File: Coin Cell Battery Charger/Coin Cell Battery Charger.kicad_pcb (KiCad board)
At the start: 4 copper layers, 120.2 x 120.2 mm, 40 parts, among them J1 0473461001, Q2 Q_PMOS_GSD, SW1 5176TRp, U1 BQ21040DBVR, U2 TLV74010PDBVR, U3 LTC6992CS6-3#TRMPBF, U4 AP2502KTR-G1, U5 AP2502KTR-G1, U6 LTC2954CTS8-1#TRMPBF

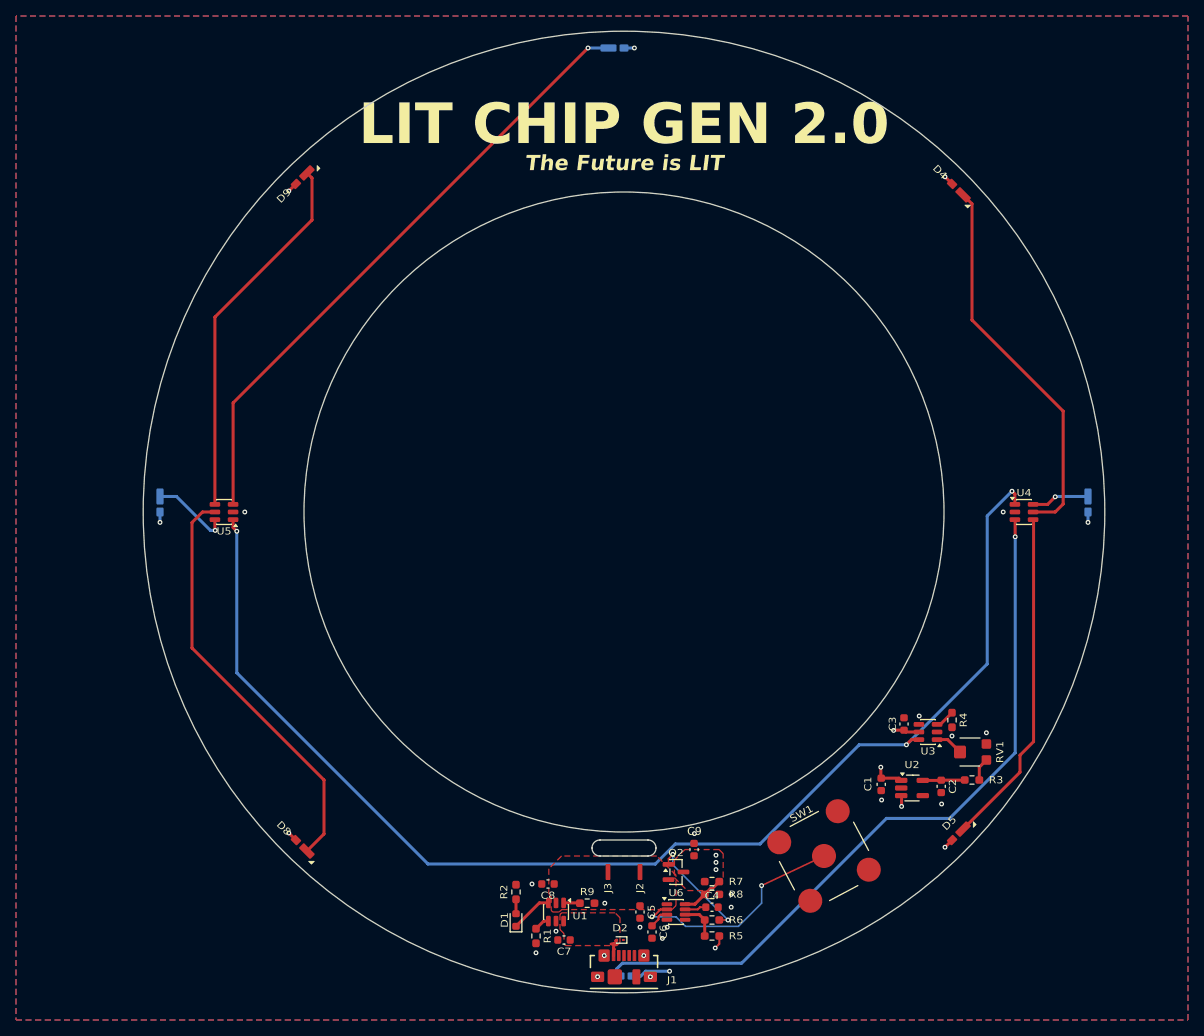
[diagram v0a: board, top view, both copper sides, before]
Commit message: Resized PCB to be 30mm OD, added vertical connector option, Electrical layout incomplete
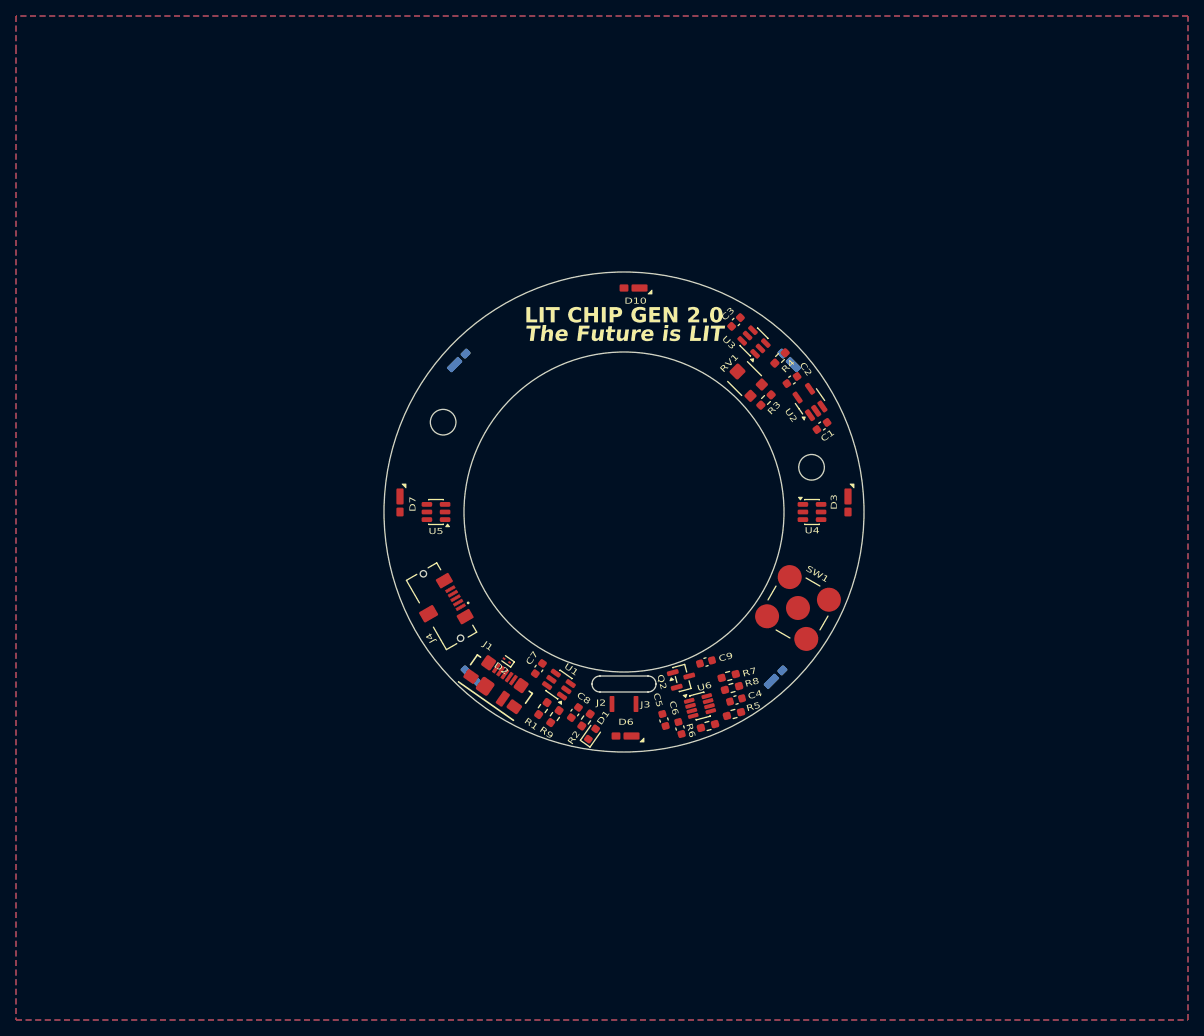
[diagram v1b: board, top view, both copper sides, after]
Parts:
- added H1: MountingHole, MountingHole:MountingHole_3.2mm_M3, F.Cu at (127.4, 88.8)
- added H2: MountingHole, MountingHole:MountingHole_3.2mm_M3, F.Cu at (173.4, 94.4)
- added J4: UJ2-MIBV-4-SMT-TR-67, _Dylan_IC:SameSky_UJ2-MIBV-4-SMT-TR-67, F.Cu at (127.2, 111.8)
- D10, D3, D6, D7: moved to F.Cu
- D4, D5, D8, D9: moved to B.Cu
- SW1: value 5176TRp -> 5136TR; footprint _Dylan_IC:Keystone_5176TR -> _Dylan_IC:Keystone_5136TR
- moved C3 54.5 mm to (164.0, 76.2), turned to 45 degrees
- moved RV1 54.4 mm to (165.2, 83.5), turned to 45 degrees
- moved C2 54.1 mm to (171.0, 83.5), turned to 35 degrees
- moved R3 54.0 mm to (167.8, 86.0), turned to -135 degrees
- moved U3 53.4 mm to (166.2, 78.8), turned to 135 degrees
- moved R4 50.1 mm to (169.5, 80.8), turned to -135 degrees
- moved U2 49.9 mm to (173.2, 86.2), turned to 125 degrees
- moved C1 45.4 mm to (174.8, 89.2), turned to 35 degrees
- moved J1 38.2 mm to (135.1, 120.3), turned to -35 degrees
- moved D2 37.7 mm to (135.4, 118.6), turned to 145 degrees
- moved C7 34.1 mm to (139.4, 119.6), turned to 55 degrees
- moved SW1 31.2 mm to (171.8, 112.0), turned to 60 degrees
- moved D6 30.1 mm to (149.0, 128.0), turned to 0 degrees
- moved D10 30.0 mm to (150.0, 72.0), turned to 0 degrees
- moved D3 30.0 mm to (178.0, 100.0)
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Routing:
- net /PWM_OUT: track 159.9 -> 0.00 mm, vias 3 -> 0
- net Net-(U4-LED4): track 91.1 -> 0.00 mm, vias 1 -> 0
- net Net-(U5-LED4): track 78.0 -> 0.00 mm, vias 1 -> 0
- net Net-(U5-LED2): track 52.2 -> 0.00 mm
- net Net-(U4-LED2): track 48.0 -> 0.00 mm
- net Net-(U5-LED3): track 46.7 -> 0.00 mm
- net Net-(U4-LED3): track 42.4 -> 0.00 mm
- net Net-(U6-~{PB}): track 28.5 -> 0.00 mm, vias 2 -> 0
- net VDD: track 22.5 -> 0.00 mm, vias 14 -> 0
- net Net-(Q2-G): track 13.6 -> 0.00 mm, vias 2 -> 0
- net Net-(U5-LED1): track 10.0 -> 0.00 mm, vias 1 -> 0
- net Net-(U4-LED1): track 7.27 -> 0.00 mm, vias 1 -> 0
- net Net-(U6-~{KILL}): track 5.45 -> 0.00 mm
- net Net-(D1-K): track 5.26 -> 0.00 mm
- net +1V0: track 5.26 -> 0.00 mm
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- removed copper zone on F.Cu, net VBATT
- removed copper zone on F.Cu, net VBUS
- removed copper zone on F.Cu, net VDD
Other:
- board size 120.2 x 120.2 mm -> 60 x 60 mm

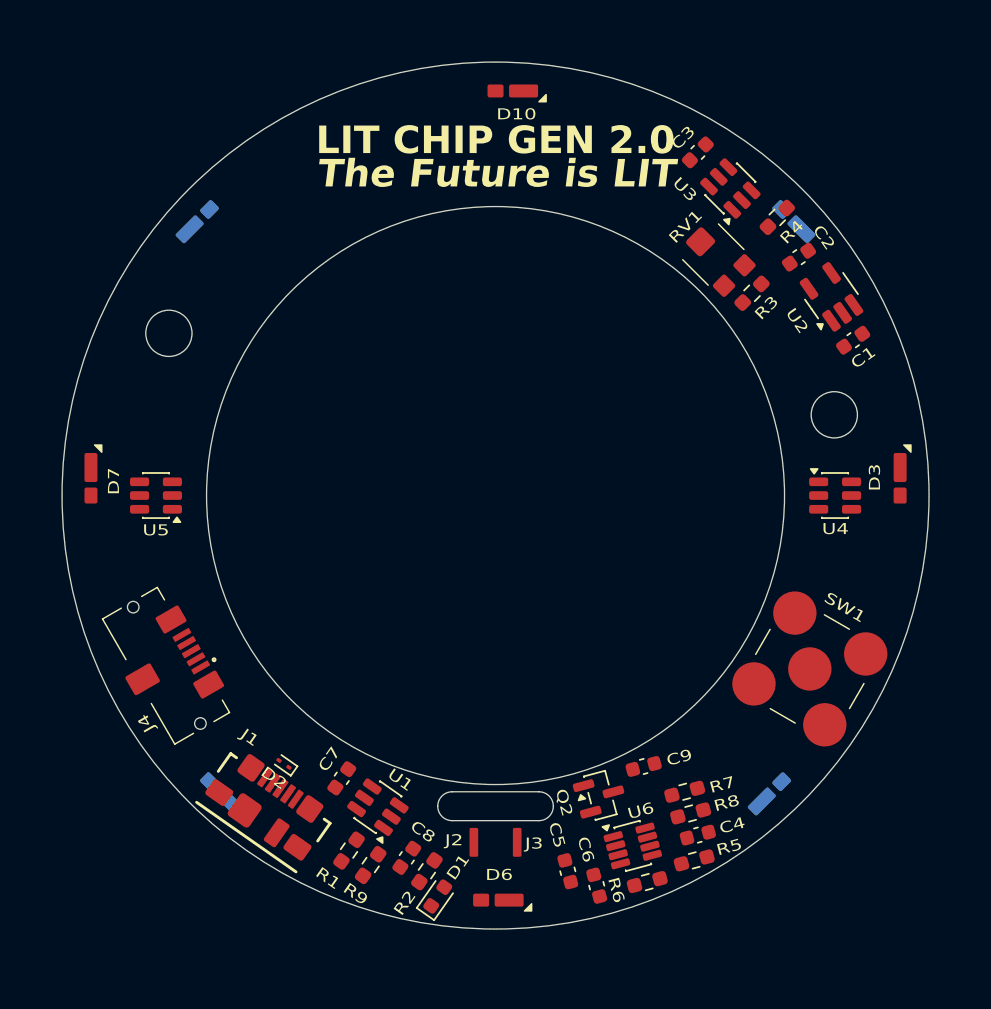
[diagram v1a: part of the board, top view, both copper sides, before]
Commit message: Finished layout for 60mm OD version
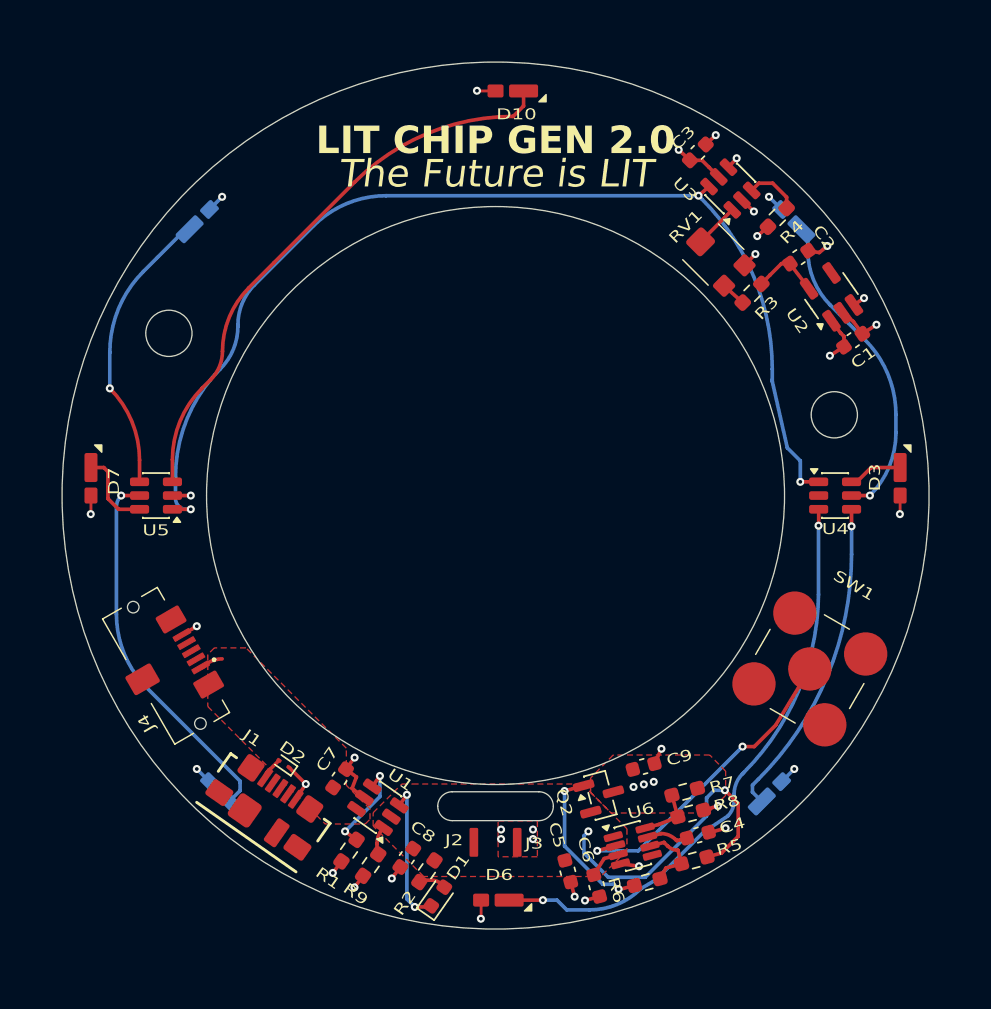
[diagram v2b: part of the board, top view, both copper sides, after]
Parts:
- moved C7 0.15 mm to (139.2, 119.6)
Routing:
- net /PWM_OUT: track 0.00 -> 75.7 mm, vias 0 -> 3
- net Net-(U4-LED4): track 0.00 -> 40.5 mm, vias 0 -> 2
- net Net-(U5-LED4): track 0.00 -> 39.4 mm
- net GND: track 0.00 -> 28.5 mm, vias 0 -> 24
- net Net-(U5-LED2): track 0.00 -> 26.0 mm, vias 0 -> 1
- net Net-(U4-LED3): track 0.00 -> 22.3 mm, vias 0 -> 1
- net Net-(U4-LED2): track 0.00 -> 22.2 mm, vias 0 -> 1
- net Net-(U6-~{PB}): track 0.00 -> 21.8 mm, vias 0 -> 2
- net VBATT: track 0.00 -> 21.5 mm, vias 0 -> 2
- net Net-(U5-LED3): track 0.00 -> 20.0 mm, vias 0 -> 1
- net VDD: track 0.00 -> 17.6 mm, vias 0 -> 14
- net Net-(Q2-G): track 0.00 -> 11.3 mm, vias 0 -> 2
- net Net-(D1-K): track 0.00 -> 10.1 mm, vias 0 -> 2
- net Net-(U1-ISET): track 0.00 -> 6.72 mm, vias 0 -> 2
- net Net-(U5-LED1): track 0.00 -> 5.65 mm
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- added copper zone on F.Cu, net VBATT
- added copper zone on F.Cu, net VBUS
- added copper zone on F.Cu, net VDD

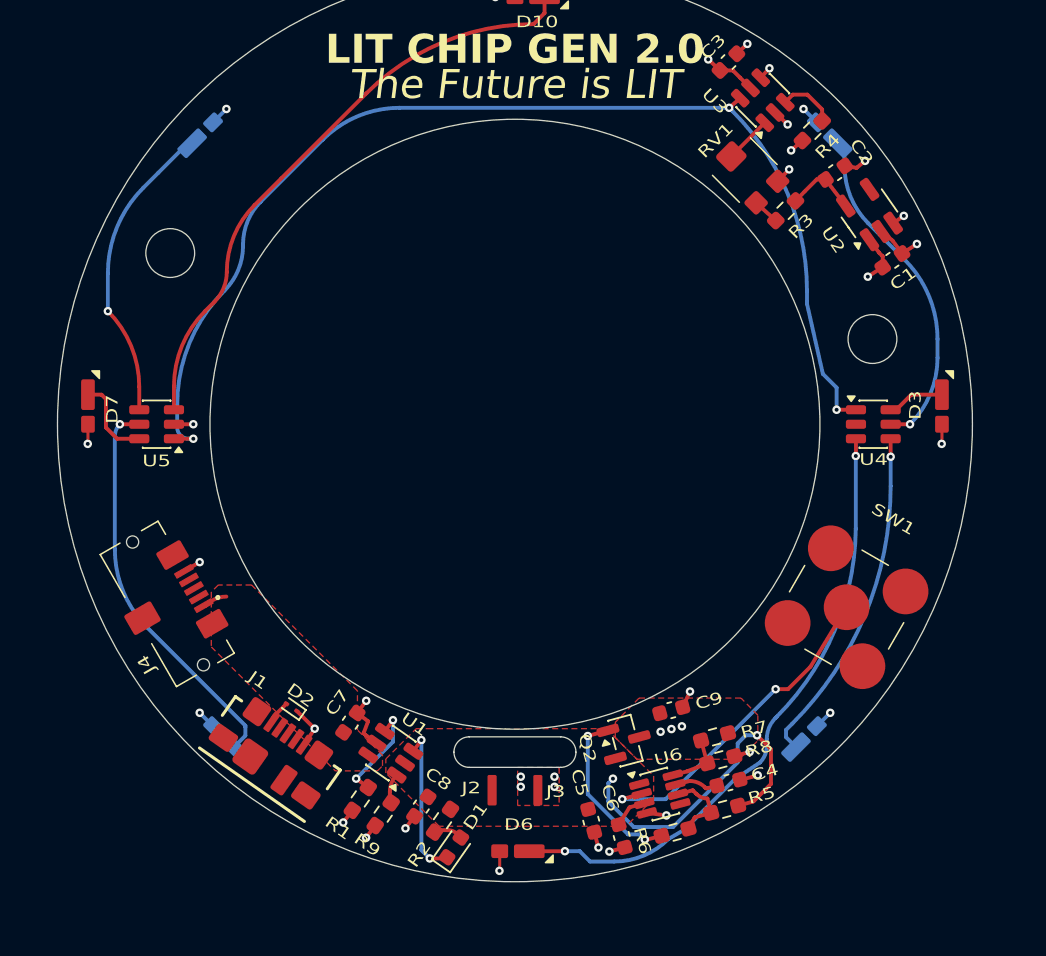
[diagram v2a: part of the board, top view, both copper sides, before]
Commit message: TP Added + M2 mounting holes
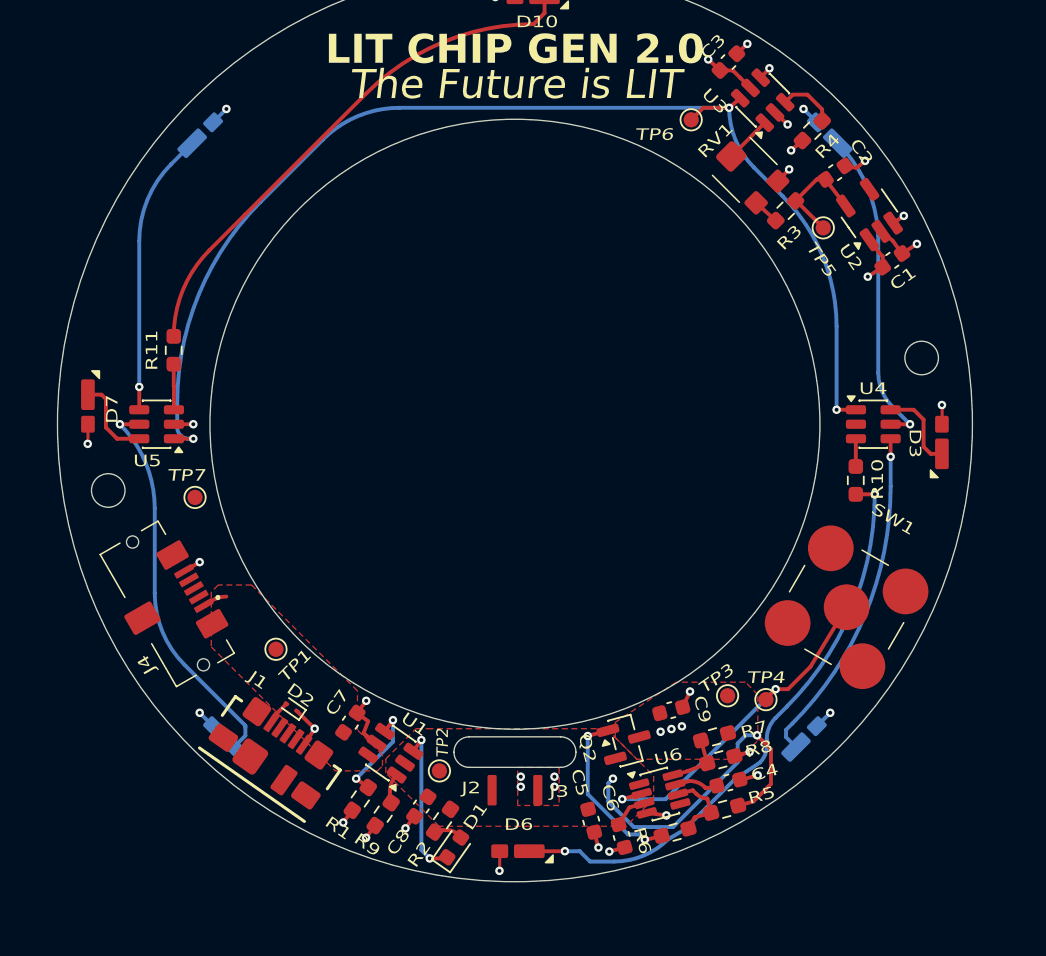
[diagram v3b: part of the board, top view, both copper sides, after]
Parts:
- added R10: 1Ω, Resistor_SMD:R_0603_1608Metric_Pad0.98x0.95mm_HandSolder, F.Cu at (172.4, 103.7)
- added R11: 1Ω, Resistor_SMD:R_0603_1608Metric_Pad0.98x0.95mm_HandSolder, F.Cu at (127.6, 95.1)
- added TP1: TestPoint, TestPoint:TestPoint_Pad_D1.0mm, F.Cu at (134.3, 114.8)
- added TP2: TestPoint, TestPoint:TestPoint_Pad_D1.0mm, F.Cu at (145.0, 122.7)
- added TP3: TestPoint, TestPoint:TestPoint_Pad_D1.0mm, F.Cu at (163.9, 117.8)
- added TP4: TestPoint, TestPoint:TestPoint_Pad_D1.0mm, F.Cu at (166.5, 118.1)
- added TP5: TestPoint, TestPoint:TestPoint_Pad_D1.0mm, F.Cu at (170.2, 87.1)
- added TP6: TestPoint, TestPoint:TestPoint_Pad_D1.0mm, F.Cu at (161.6, 80.0)
- added TP7: TestPoint, TestPoint:TestPoint_Pad_D1.0mm, F.Cu at (129.0, 104.8)
- H1, H2: footprint MountingHole:MountingHole_3.2mm_M3 -> MountingHole:MountingHole_2.2mm_M2_ISO14580
- moved H1 16.1 mm to (123.3, 104.3)
- moved H2 3.46 mm to (176.7, 95.7)
- turned D3 to -90 degrees
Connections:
- D10 pad 2: Net-(U5-LED4) -> Net-(D10-Pad2)
- D6 pad 2: Net-(U4-LED4) -> Net-(D6-Pad2)
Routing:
- net Net-(U4-LED4): track 40.5 -> 1.82 mm, vias 2 -> 0
- net Net-(D6-Pad2): track 0.00 -> 38.5 mm, vias 0 -> 2
- net Net-(U5-LED4): track 39.4 -> 3.00 mm
- net Net-(D10-Pad2): track 0.00 -> 34.9 mm
- net /PWM_OUT: track 75.7 -> 78.7 mm
- net +1V0: track 4.75 -> 7.31 mm
- net Net-(U4-LED1): track 3.77 -> 5.60 mm
- net Net-(U5-LED3): track 20.0 -> 18.6 mm
- net Net-(U4-LED2): track 22.2 -> 21.1 mm
- net Net-(U6-~{PB}): track 21.8 -> 22.8 mm
- net Net-(U5-LED2): track 26.0 -> 25.5 mm
